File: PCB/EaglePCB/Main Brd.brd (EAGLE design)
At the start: 91.4 x 48.3 mm, 9 parts, among them J1 1909763-1, J2 1909763-1, U1 ATWINC1500-MR210PB1952-T, U2 ENC28J60-I/SP, U3 MSP430FR2355TDBTRDBT0038A_M, U4 SX1272IMLTRT, U5 SX1272IMLTRT, U6 ARJM11C7-114-BA-EW2

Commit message: LoRa Antenna + Ethernet routing
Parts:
- removed J2: 1909763-1, 473:CONN3_1909763_TEC
- added 10NH-ANT1, 10NH-ANT2, C1, R1: (no value), microbuilder:0402
- added ANT1-ANT2\, ANT1-ANT2\1: 8.2nH, microbuilder:_0402
- added ANT1-GND, ANT1-GND1, ANT2-GND, ANT2-GND1, ANT2-GND2, ANT2-GND3: 4.7pF, microbuilder:0402
- added ANT2-ANT1, ANT2-ANT3: 7.5nH, microbuilder:_0402
- added J3: 1909763-1, 473:CONN3_1909763_TEC
- added L2: (no value), microbuilder:_0402
- added RFI-GND, RFI-GND1: 5.6 nH, microbuilder:_0402
- added RFI-RFO, RFI-RFO1: 1.5pF 50v Cer, microbuilder:0402
- added RFO-33PF, RFO-33PF1: 10nH, microbuilder:_0402
- added RFO-VR_PA, RFO-VR_PA1, VR_PA-PA_BOOST, VR_PA-PA_BOOST1: 33nH, microbuilder:_0402
- renumbered U4 to LORA2, U5 to LORA1
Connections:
- new net ANT1: 10NH-ANT1.1, ANT1-ANT2\.2, ANT1-GND.2
- new net ANT1-2: 10NH-ANT2.1, ANT1-ANT2\1.2, ANT1-GND1.2
- new net ANT2: ANT1-ANT2\.1, ANT2-ANT3.2, ANT2-GND.2
- new net ANT2-2: ANT1-ANT2\1.1, ANT2-ANT1.2, ANT2-GND2.2
- new net ANT3: ANT2-ANT3.1, ANT2-GND1.2, J1.1
- new net ANT3-2: ANT2-ANT1.1, ANT2-GND3.2, J3.1
- new net GND: ANT1-GND.1, ANT1-GND1.1, ANT2-GND.1, ANT2-GND1.1, ANT2-GND2.1, ANT2-GND3.1, J1.2, J1.3, J3.2, J3.3, LORA1.16, LORA1.22, LORA1.26, LORA1.29, LORA2.16, LORA2.22, LORA2.26, LORA2.29, RFI-GND.2, RFI-GND1.2
- new net N$1: 10NH-ANT1.2, RFO-33PF.1
- new net N$2: 10NH-ANT2.2, RFO-33PF1.1
- new net PA_BOOST: LORA1.27, VR_PA-PA_BOOST.1
- new net PA_BOOST2: LORA2.27, VR_PA-PA_BOOST1.1
- new net RFI: LORA1.25, RFI-GND.1, RFI-RFO.1
- new net RFI2: LORA2.25, RFI-GND1.1, RFI-RFO1.1
- new net RFO: LORA1.24, RFI-RFO.2, RFO-33PF.2, RFO-VR_PA.2
- new net RFO2: LORA2.24, RFI-RFO1.2, RFO-33PF1.2, RFO-VR_PA1.2
- new net VR_PA: LORA1.28, RFO-VR_PA.1, VR_PA-PA_BOOST.2
- new net VR_PA2: LORA2.28, RFO-VR_PA1.1, VR_PA-PA_BOOST1.2

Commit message: updated ethernet
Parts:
- added LEDG, LEDY: (no value), microbuilder:0402
- added RD-GND, RD-GND1: 0.1 uF, microbuilder:0402
- added RDM-GND, RDM-GND1: 49.9 Ohm', microbuilder:0402
- added RDP-GND, RDP-GND1: 49.9 Ohm, microbuilder:0402
- added TCT-3V3: (no value), microbuilder:0603
- added VC2ETH-GND, VC2PETH-GND: 75 Ohm, microbuilder:0402
- added VC2ETH-GNDC, VC2PETH-GNDC: 1nF, microbuilder:0402
- added VCAPCLOSE: 10 uF, microbuilder:0805
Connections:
- removed net VC1+: U6.7
- removed net VC1-: U6.2
- removed net VC2+: U6.6
- removed net VC2-: U6.1
- new net 3V3: LEDG.2, LEDY.2, TCT-3V3.2
- new net LEDGN: U2.28, U6.12
- new net LEDYN: U6.14
- new net LEDYP: U2.27
- new net N$3: U6.4
- new net N$4: U2.1, VCAPCLOSE.2
- new net N$5: VC2ETH-GND.1, VC2ETH-GNDC.2
- new net N$6: VC2PETH-GND.1, VC2PETH-GNDC.2
- new net N$7: LEDY.1, U6.13
- new net N$8: RD-GND.1, RDM-GND.1, RDP-GND.1
- new net N$9: LEDG.1, U6.11
- new net RDM: RDM-GND.2, U2.12, U6.3
- new net RDP: RDP-GND.2, U2.13, U6.5
- new net TDC: RD-GND1.1, RDM-GND1.1, RDP-GND1.1, TCT-3V3.1, U6.9
- new net TDM: RDM-GND1.2, U2.16, U6.8
- new net TDP: RDP-GND1.2, U2.17, U6.10
- new net VC2ETH: U6.1, VC2ETH-GND.2
- new net VC2PETH: U6.6, VC2PETH-GND.2
- net GND: now also RD-GND.2, RD-GND1.2, U6.2, U6.7, VC2ETH-GNDC.1, VC2PETH-GNDC.1, VCAPCLOSE.1

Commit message: added eth power coupling and Osc circuit
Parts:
- added OSC1-GND, OSC2-GND: 16 pF, microbuilder:0603
- added RBIAS-GNDCLOSE: 2.32K 1%, Resistor_Capacitor:RES_0603
- added U$2: CRYSTAL, 473:4-SMD-PACKAGE
- added VSS-VDD_ETH, VSSOSC-VDDOSC, VSSPLL-VDDPLL, VSSRX-VDDRX, VSSTX-VDDTX: 0.1 uF, microbuilder:0603
- RD-GND, RD-GND1: device microbuilder:0402 -> microbuilder:0603
- moved RD-GND1 38.9 mm to (-0.85, -153.7)
- moved RD-GND 34.0 mm to (-0.85, -141.0)
- renumbered U2 to ETH
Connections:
- new net N$10: ETH.14, RBIAS-GNDCLOSE.2
- new net OSC1_ETH: ETH.23, OSC1-GND.1, U$2.P$1
- new net OSC2_ETH: ETH.24, OSC2-GND.1, U$2.P$4
- new net VDDOSC_ETH: ETH.25, VSSOSC-VDDOSC.1
- new net VDDPLL_ETH: ETH.20, VSSPLL-VDDPLL.1
- new net VDDRX_ETH: ETH.19, VSSRX-VDDRX.2
- new net VDDTX_ETH: ETH.15, VSSTX-VDDTX.2
- new net VDD_ETH: ETH.28, VSS-VDD_ETH.2
- new net VSSOSC_ETH: ETH.22, VSSOSC-VDDOSC.2
- new net VSSPLL_ETH: ETH.21, VSSPLL-VDDPLL.2
- new net VSSRX_ETH: ETH.11, VSSRX-VDDRX.1
- new net VSSTX_ETH: ETH.18, VSSTX-VDDTX.1
- new net VSS_ETH: ETH.2, VSS-VDD_ETH.1
- net GND: now also OSC1-GND.2, OSC2-GND.2, RBIAS-GNDCLOSE.1
- net LEDGN: now also ETH.27; no longer ETH.28
- net LEDYP: now also ETH.26; no longer ETH.27

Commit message: removed LED group
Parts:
- removed D1: 5700100132F, 473:LED_5700100132F
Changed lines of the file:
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@@
 <attribute name="VALUE" x="69.3928" y="8.255" size="1.27" layer="21" ratio="6" rot="SR0"/>
-</element>
-<element name="D1" library="473" package="LED_5700100132F" value="5700100132F" x="8.89" y="29.21" smashed="yes">
-<attribute name="DESCRIPTION" value=" LED Circuit Board Indicator LED Circuit Board Indicator 3 High Green (x 1), Red (x 1), Yellow (x 1) Diffused 2.2V Green, 2V Red, 2.1V Yellow 25mA Green, 30mA Red, 30mA Yellow Round with Domed Top 2.00mm Dia Through Hole, Right Angle " x="8.89" y="29.21" size="1.778" layer="27" display="off"/>
-<attribute name="DIGI-KEY_PART_NUMBER" value="350-1809-ND" x="8.89" y="29.21" size="1.778" layer="27" display="off"/>
-<attribute name="MF" value="Dialight" x="8.89" y="29.21" size="1.778" layer="27" display="off"/>
-<attribute name="MP" value="5700100132F" x="8.89" y="29.21" size="1.778" layer="27" display="off"/>
-<attribute name="NAME" x="0.39" y="32.71" size="1.27" layer="25"/>
-<attribute name="PACKAGE" value="None" x="8.89" y="29.21" size="1.778" layer="27" display="off"/>
-<attribute name="PURCHASE-URL" value="https://pricing.snapeda.com/search/part/5700100132F/?ref=eda" x="8.89" y="29.21" size="1.778" layer="27" display="off"/>
-<attribute name="VALUE" x="0.39" y="26.21" size="1.27" layer="27" align="top-left"/>
 </element>
 <element name="LORA1" library="473" package="QFN28_6X6_SEM" value="SX1272IMLTRT" x="64.77" y="20.32" smashed="yes">

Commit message: adjusted crystal oscillator values
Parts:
- OSC1-GND: value 16 pF -> 14pF
- OSC2-GND: value 16 pF -> 180 pF
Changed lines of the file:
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@@
 </element>
 <element name="U$2" library="473" package="4-SMD-PACKAGE" value="CRYSTAL" x="-8.89" y="-168.91" smashed="yes"/>
-<element name="OSC2-GND" library="microbuilder" package="0603" value="16 pF" x="-8.89" y="-171.45" smashed="yes">
+<element name="OSC2-GND" library="microbuilder" package="0603" value="180 pF" x="-8.89" y="-171.45" smashed="yes">
 <attribute name="NAME" x="-7.112" y="-171.577" size="0.8128" layer="25" font="vector" ratio="18"/>
 <attribute name="VALUE" x="-7.112" y="-172.212" size="0.4064" layer="27" font="vector" ratio="10"/>
 </element>
-<element name="OSC1-GND" library="microbuilder" package="0603" value="16 pF" x="-8.89" y="-173.99" smashed="yes">
+<element name="OSC1-GND" library="microbuilder" package="0603" value="14pF" x="-8.89" y="-173.99" smashed="yes">
 <attribute name="NAME" x="-7.112" y="-174.117" size="0.8128" layer="25" font="vector" ratio="18"/>
 <attribute name="VALUE" x="-7.112" y="-174.752" size="0.4064" layer="27" font="vector" ratio="10"/>

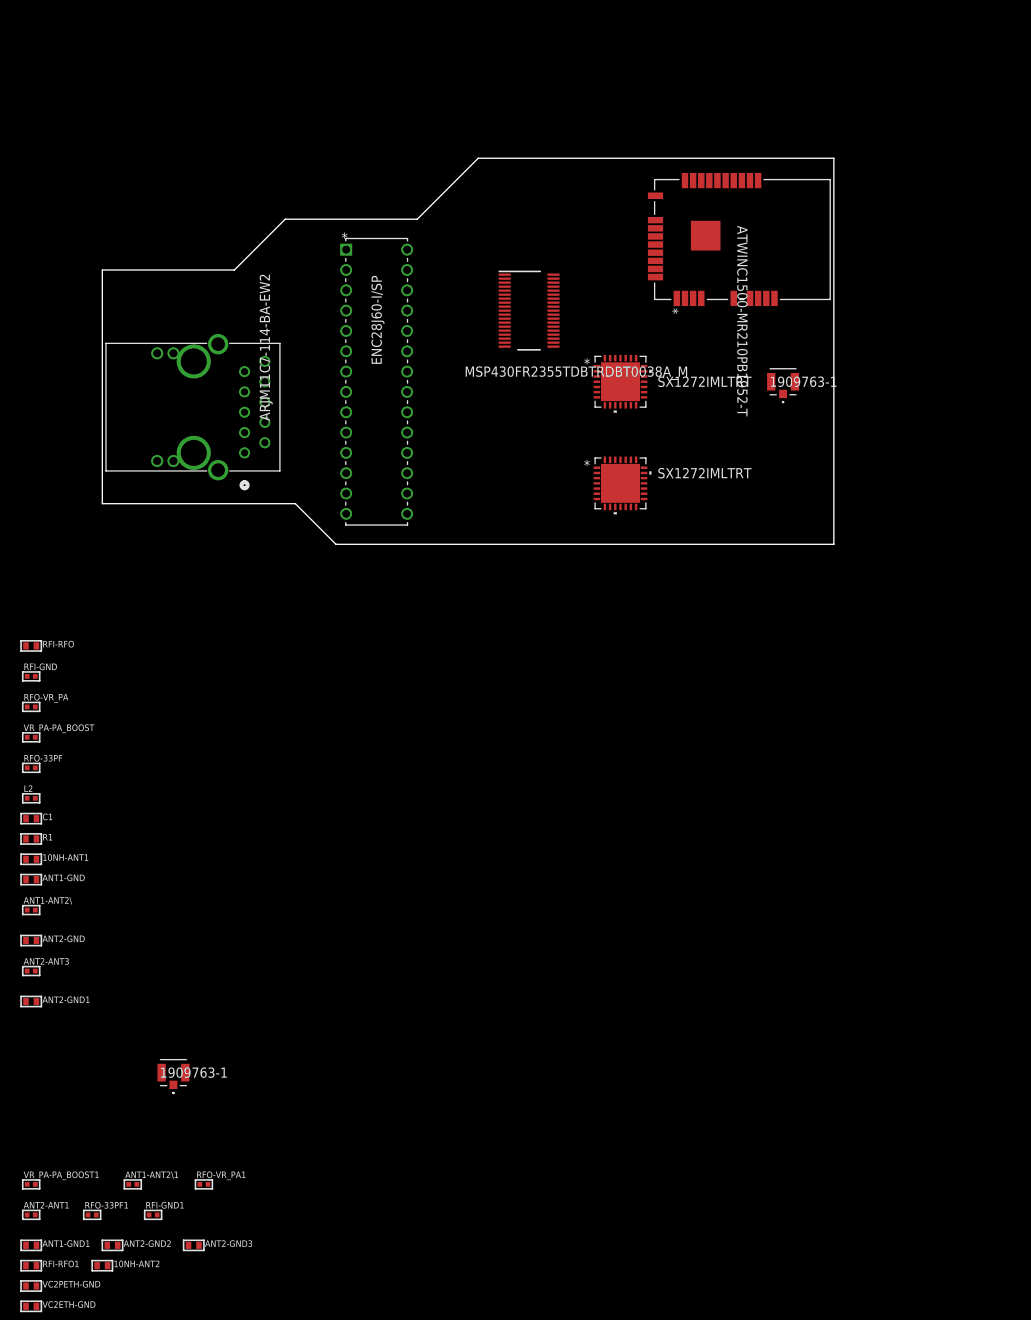
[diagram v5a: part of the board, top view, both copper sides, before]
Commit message: Antenna's Arranged
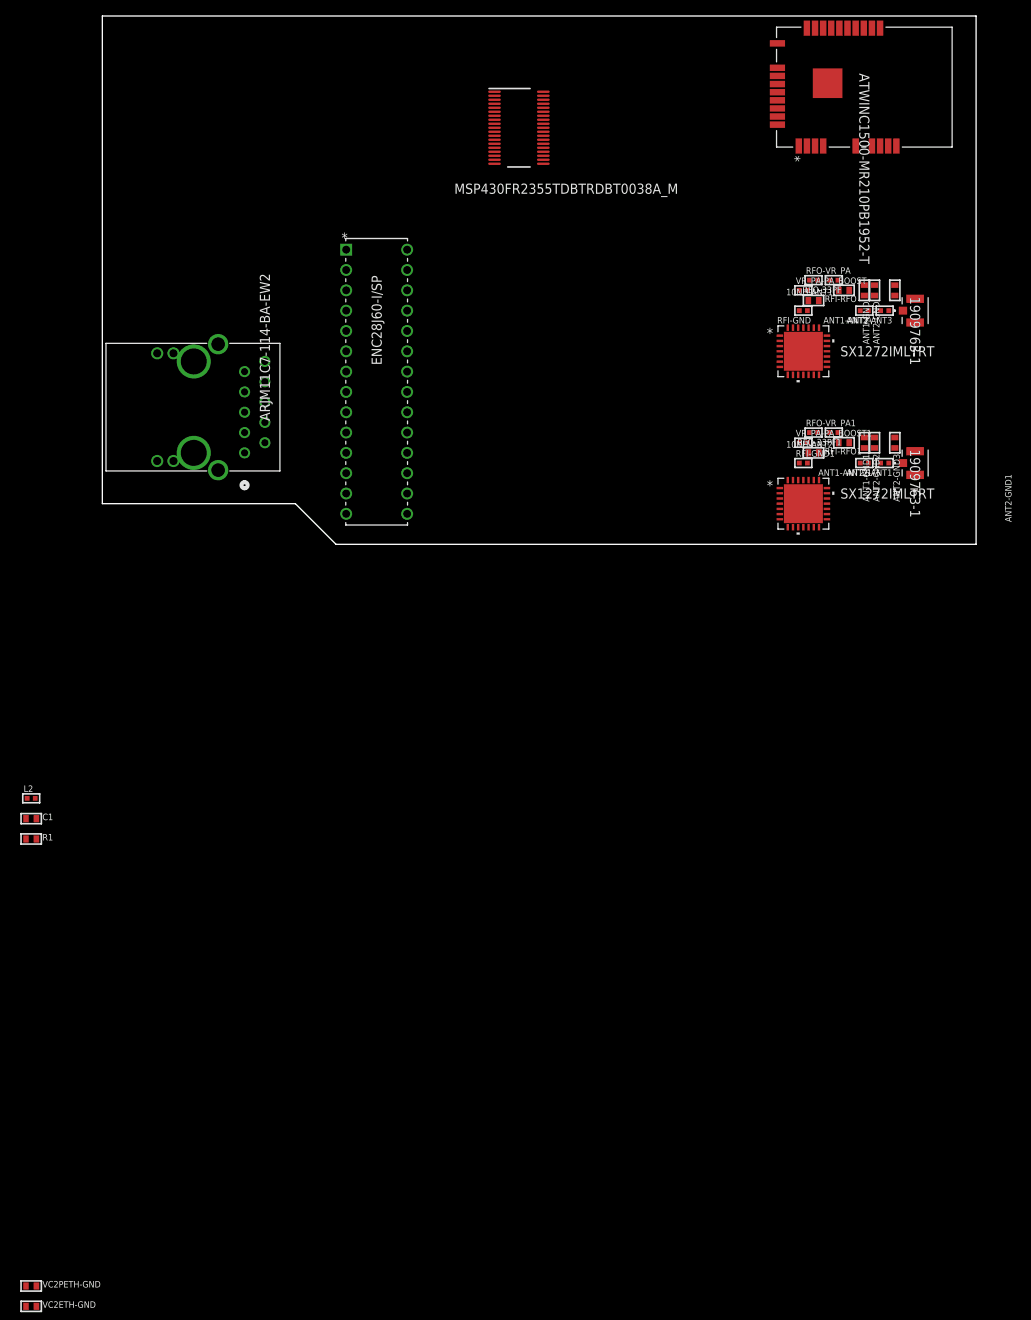
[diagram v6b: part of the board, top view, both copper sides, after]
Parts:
- moved ANT1-GND1 144.6 mm to (95.2, 12.7), turned to 270 degrees
- moved ANT2-ANT1 142.2 mm to (97.8, 10.2), turned to 180 degrees
- moved RFI-RFO1 141.0 mm to (88.9, 11.4)
- moved ANT2-GND1 139.8 mm to (99.1, 31.8), turned to 270 degrees
- moved 10NH-ANT2 138.5 mm to (92.7, 12.7), turned to 180 degrees
- moved ANT2-GND2 138.3 mm to (96.5, 12.7), turned to 270 degrees
- moved ANT2-ANT3 134.9 mm to (97.8, 29.2), turned to 180 degrees
- moved RFO-33PF1 134.8 mm to (91.4, 14.0), turned to 180 degrees
- moved VR_PA-PA_BOOST1 133.8 mm to (87.6, 12.7)
- moved ANT2-GND3 133.2 mm to (99.1, 12.7), turned to 270 degrees
- moved ANT2-GND 133.1 mm to (96.5, 31.8), turned to 270 degrees
- moved ANT1-ANT2\1 128.4 mm to (95.2, 10.2), turned to 180 degrees
- moved ANT1-ANT2\ 128.3 mm to (95.2, 29.2), turned to 180 degrees
- moved ANT1-GND 127.6 mm to (95.2, 31.8), turned to 270 degrees
- moved RFI-GND1 124.3 mm to (87.6, 10.2)
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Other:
- board size 91.4 x 48.3 mm -> 109.2 x 66 mm

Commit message: Ethernet Layout
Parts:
- moved OSC1-GND 208.9 mm to (53.3, 25.4), turned to 90 degrees
- moved OSC2-GND 205.0 mm to (48.3, 25.4), turned to 90 degrees
- moved U$2 200.8 mm to (50.8, 22.9), turned to 180 degrees
- moved VSSPLL-VDDPLL 194.9 mm to (58.4, 16.5), flipped to the bottom
- moved VSSOSC-VDDOSC 188.8 mm to (50.8, 15.2), flipped to the bottom, turned to 180 degrees
- moved VSSRX-VDDRX 188.4 mm to (63.5, 15.2), flipped to the bottom, turned to 90 degrees
- moved VSSTX-VDDTX 188.1 mm to (68.6, 15.2), flipped to the bottom, turned to 180 degrees
- moved VSS-VDD_ETH 183.3 mm to (40.6, 15.2), flipped to the bottom, turned to 90 degrees
- moved RD-GND1 180.2 mm to (28.4, 24.1)
- moved RD-GND 163.6 mm to (70.3, 6.35)
- moved RBIAS-GNDCLOSE 159.4 mm to (72.4, 8.89), turned to 90 degrees
- moved LEDY 153.4 mm to (8.89, 26.7), turned to 90 degrees
- moved TCT-3V3 147.5 mm to (25.4, 25.4), turned to 90 degrees
- moved RDP-GND1 140.1 mm to (25.4, 22.9)
- moved RDP-GND 138.8 mm to (69.8, 8.89), turned to 90 degrees
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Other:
- outline, holes or cut-outs redrawn

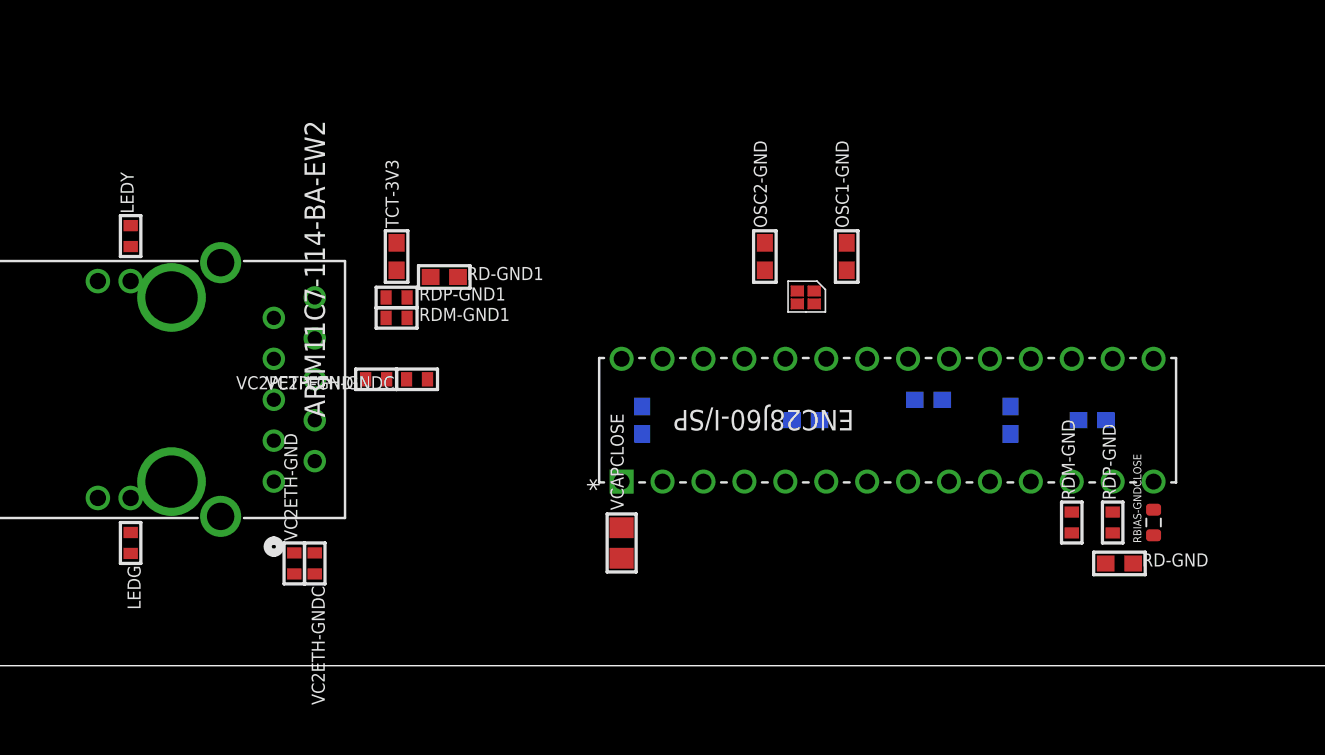
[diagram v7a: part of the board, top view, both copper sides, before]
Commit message: edited ethernet with minor routing
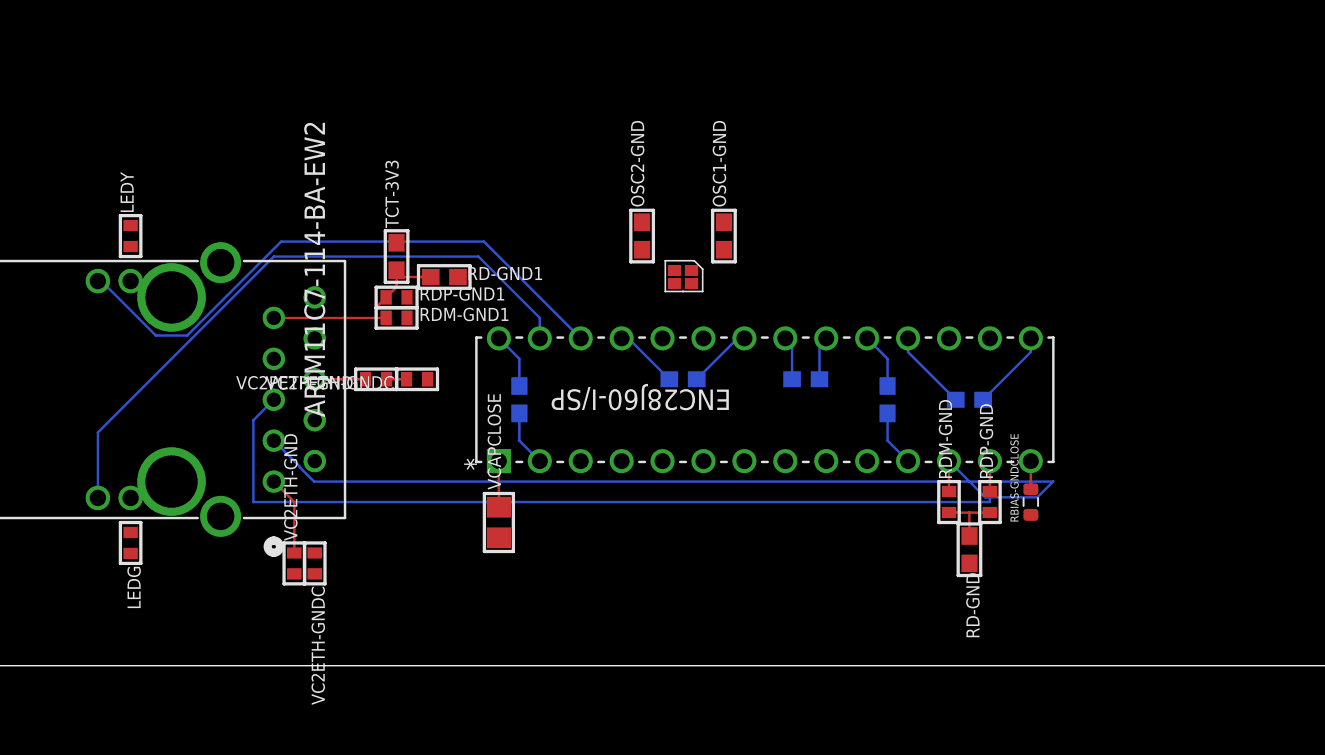
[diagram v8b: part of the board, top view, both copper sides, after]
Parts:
- moved RD-GND 9.35 mm to (61.0, 7.20), turned to 270 degrees
- moved VSSOSC-VDDOSC 8.03 mm to (43.2, 17.8)
- moved OSC1-GND 7.73 mm to (45.7, 26.7)
- moved RBIAS-GNDCLOSE 7.73 mm to (64.8, 10.2)
- moved RDM-GND 7.73 mm to (59.7, 10.2)
- moved VSSPLL-VDDPLL 7.73 mm to (50.8, 17.8)
- moved OSC2-GND 7.73 mm to (40.6, 26.7)
- moved VCAPCLOSE 7.73 mm to (31.8, 8.89)
- moved VSS-VDD_ETH 7.73 mm to (33.0, 16.5)
- moved VSSRX-VDDRX 7.73 mm to (55.9, 16.5)
- moved VSSTX-VDDTX 7.73 mm to (61.0, 16.5)
- moved ETH 7.73 mm to (31.8, 12.7)
- moved RDP-GND 7.73 mm to (62.2, 10.2)
- moved U$2 7.73 mm to (43.2, 24.1)
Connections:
- removed net LEDYP: ETH.26
- net LEDYN: now also ETH.26
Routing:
- net RDM: track 0.00 -> 59.1 mm
- net RDP: track 0.00 -> 57.0 mm
- net LEDGN: track 0.00 -> 38.9 mm
- net LEDYN: track 0.00 -> 36.3 mm
- net TDC: track 0.00 -> 12.7 mm
- net VSSTX_ETH: track 0.00 -> 5.04 mm
- net VDDTX_ETH: track 0.00 -> 5.04 mm
- net VC2ETH: track 0.00 -> 4.96 mm
- net VSSOSC_ETH: track 0.00 -> 4.01 mm
- net VDDOSC_ETH: track 0.00 -> 4.01 mm
- net N$8: track 0.00 -> 4.00 mm
- net VDD_ETH: track 0.00 -> 3.49 mm
- net VDDRX_ETH: track 0.00 -> 3.49 mm
- net VSS_ETH: track 0.00 -> 3.49 mm
- net VSSRX_ETH: track 0.00 -> 3.49 mm
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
